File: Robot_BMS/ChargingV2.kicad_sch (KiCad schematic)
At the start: 11 parts, among them Q7 2N7002, U4 TPS54308DDCR

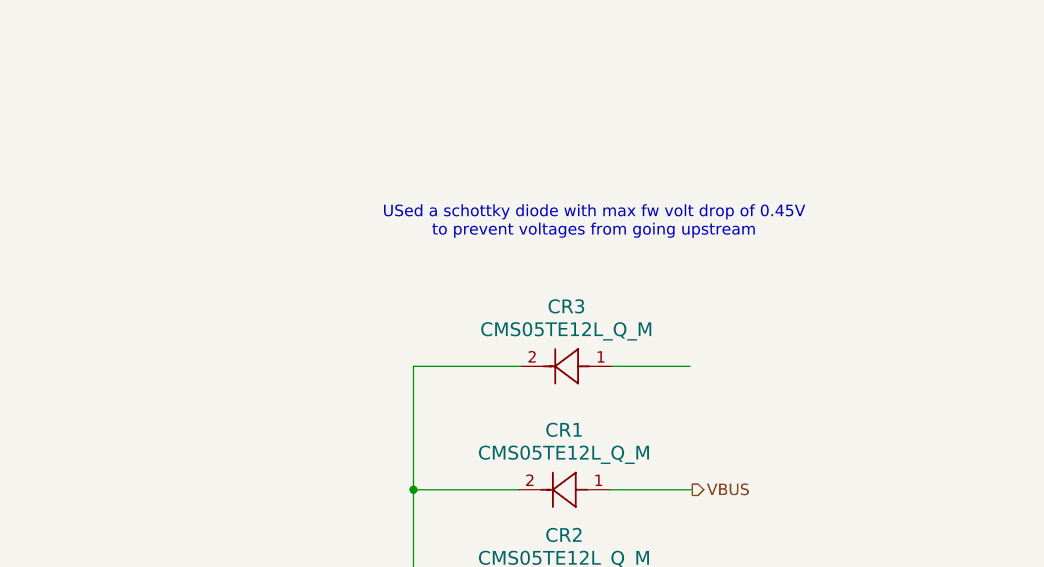
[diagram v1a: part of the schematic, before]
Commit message: battery management ic is being added
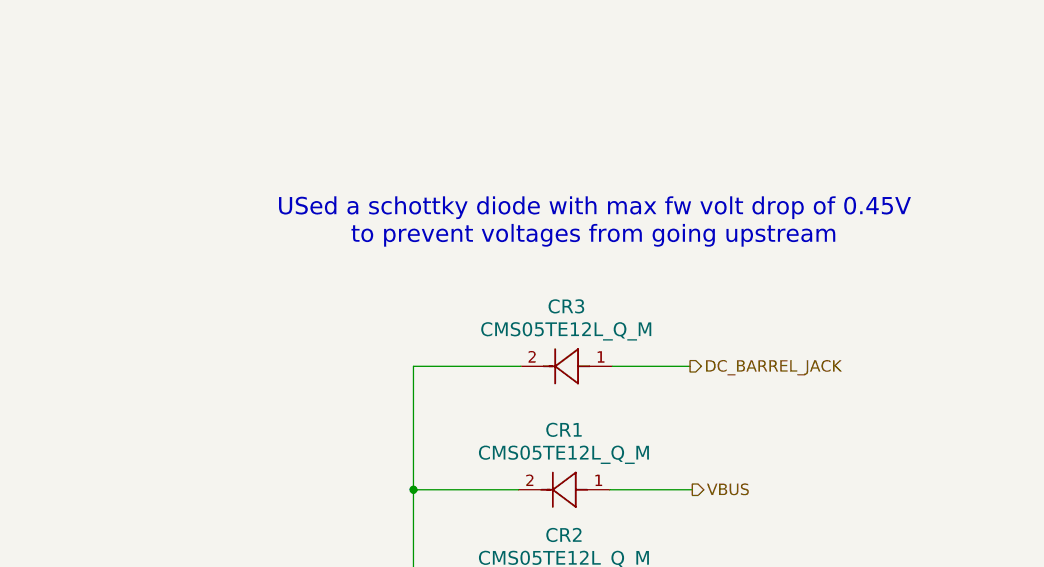
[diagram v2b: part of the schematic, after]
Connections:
- net DC_BARREL_JACK: now reaches CR3.1
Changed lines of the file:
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@@
 		(effects
 			(font
-				(size 1.27 1.27)
+				(size 1.905 1.905)
 			)
 		)
@@
 		)
 	)
+	(hierarchical_label "DC_BARREL_JACK"
+		(shape output)
+		(at 237.236 82.804 0)
+		(effects
+			(font
+				(size 1.27 1.27)
+			)
+			(justify left)
+		)
+	)

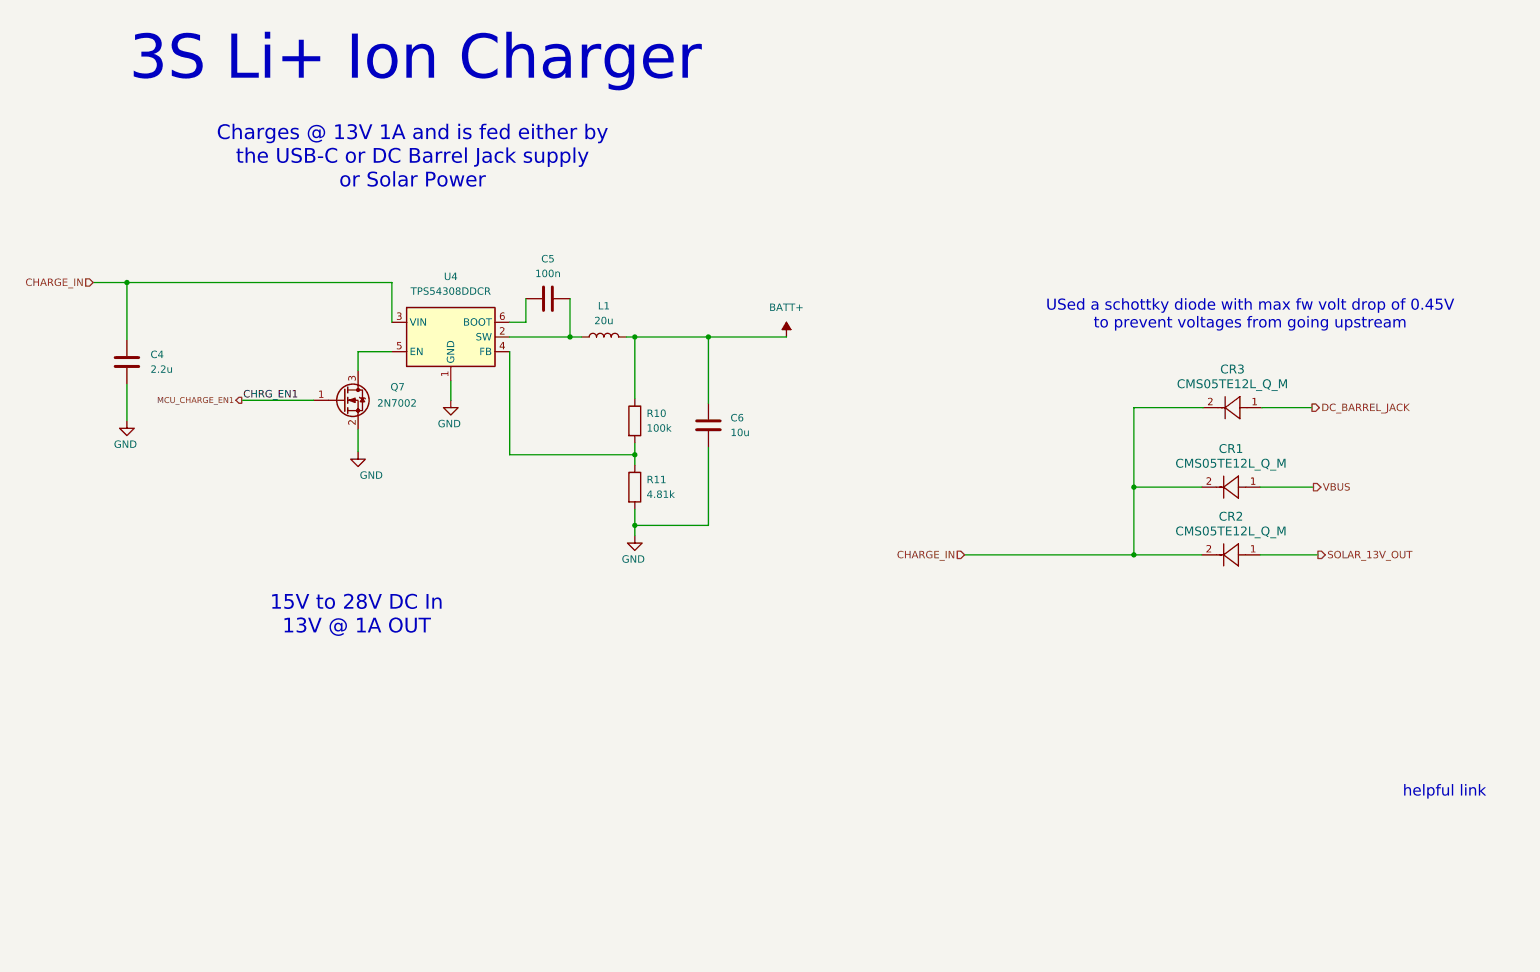
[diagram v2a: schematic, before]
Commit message: System drawing down on top schematic, will start inputting footprints
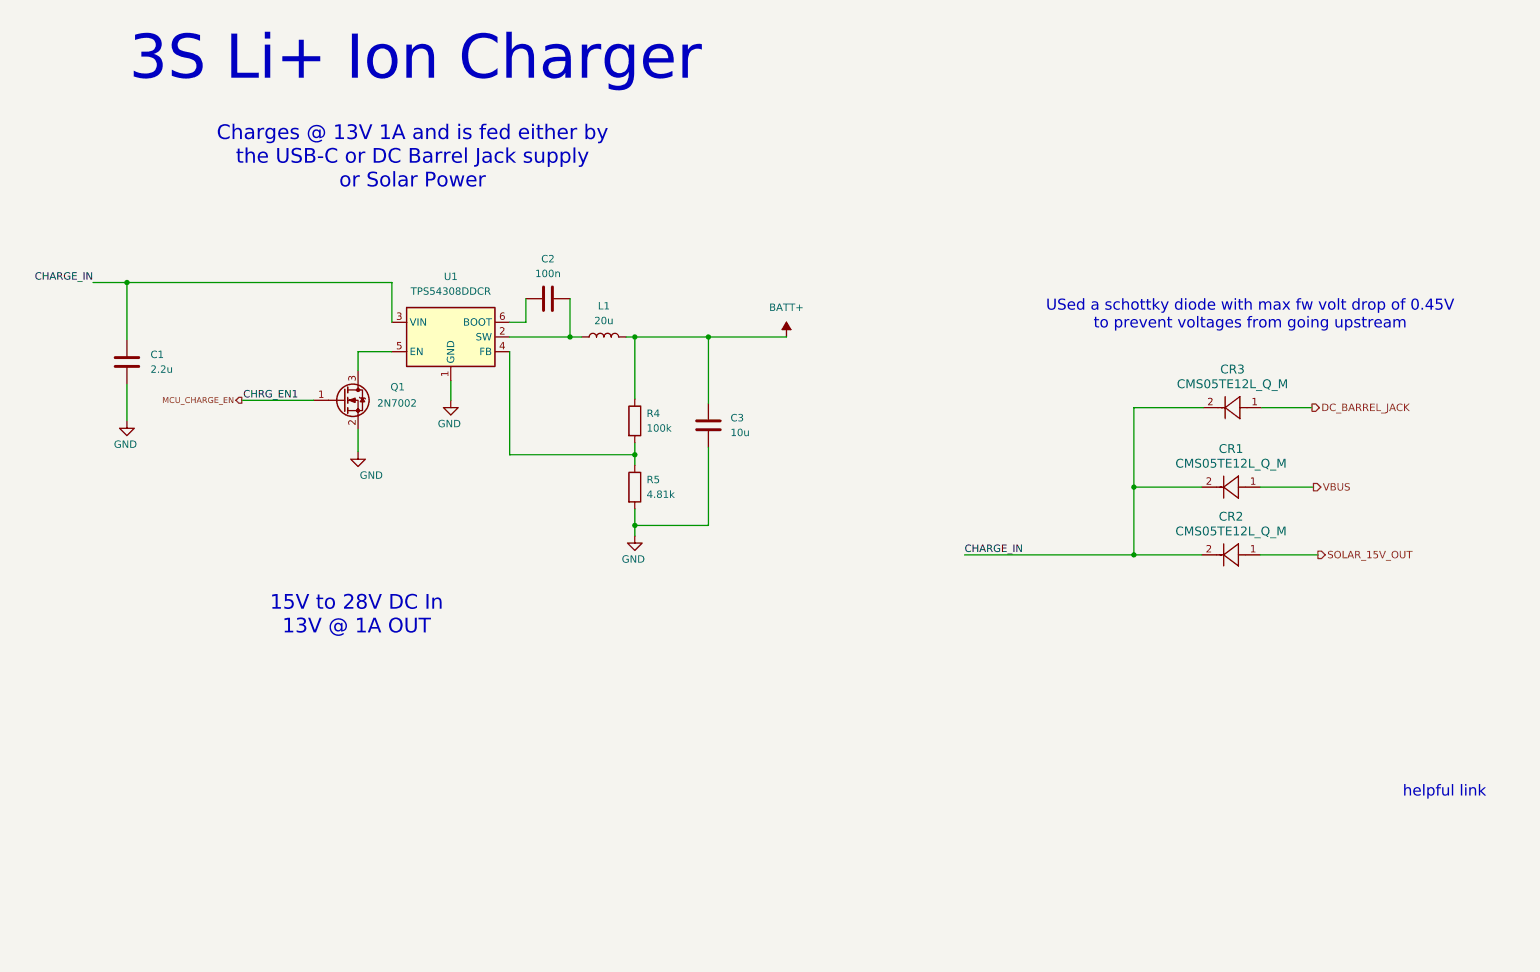
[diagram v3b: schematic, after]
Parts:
- renumbered C4 to C1, C5 to C2, C6 to C3, Q7 to Q1, R10 to R4, R11 to R5, U4 to U1
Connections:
- net MCU_CHARGE_EN1 renamed MCU_CHARGE_EN
- net SOLAR_13V_OUT renamed SOLAR_15V_OUT
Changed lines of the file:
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@@
 		)
 	)
-	(hierarchical_label "SOLAR_13V_OUT"
+	(label "CHARGE_IN"
+		(at 177.292 108.204 0)
+		(effects
+			(font
+				(size 1.27 1.27)
+			)
+			(justify left bottom)
+		)
+	)
+	(label "CHARGE_IN"
+		(at 26.924 61.214 180)
+		(effects
+			(font
+				(size 1.27 1.27)
+			)
+			(justify right bottom)
+		)
+	)
+	(hierarchical_label "SOLAR_15V_OUT"
 		(shape output)
 		(at 238.252 108.204 0)
@@
 		)
 	)
-	(hierarchical_label "MCU_CHARGE_EN1"
+	(hierarchical_label "MCU_CHARGE_EN"
 		(shape output)
 		(at 52.578 81.534 180)
@@
 			(font
 				(size 1.016 1.016)
-			)
-			(justify right)
-		)
-	)
-	(hierarchical_label "CHARGE_IN"
-		(shape input)
-		(at 177.292 108.204 180)
-		(effects
-			(font
-				(size 1.27 1.27)
 			)
 			(justify right)
@@
 		)
 	)
-	(hierarchical_label "CHARGE_IN"
-		(shape input)
-		(at 26.924 61.214 180)
-		(effects
-			(font
-				(size 1.27 1.27)
-			)
-			(justify right)
-		)
-	)
 	(symbol
 		(lib_id "Regulator_Switching:TPS54308")
@@
 		(dnp no)
 		(fields_autoplaced yes)
-		(property "Reference" "U4"
+		(property "Reference" "U1"
 			(at 88.646 60.198 0)
 			(effects
@@
 			(project ""
 				(path "/72551b1c-3d40-4199-8911-e5b015f4abec/31837631-dd5f-49d4-a8ae-a36c80dc2ea1"
-					(reference "U4")
+					(reference "U1")
 					(unit 1)
 				)
@@
 		(dnp no)
 		(fields_autoplaced yes)
-		(property "Reference" "C5"
+		(property "Reference" "C2"
 			(at 105.41 57.15 90)
 			(effects
@@
 			(project ""
 				(path "/72551b1c-3d40-4199-8911-e5b015f4abec/31837631-dd5f-49d4-a8ae-a36c80dc2ea1"
-					(reference "C5")
+					(reference "C2")
 					(unit 1)
 				)
@@
 		(dnp no)
 		(fields_autoplaced yes)
-		(property "Reference" "C6"
+		(property "Reference" "C3"
 			(at 136.906 84.5819 0)
 			(effects
@@
 			(project ""
 				(path "/72551b1c-3d40-4199-8911-e5b015f4abec/31837631-dd5f-49d4-a8ae-a36c80dc2ea1"
-					(reference "C6")
+					(reference "C3")
 					(unit 1)
 				)
@@
 		(dnp no)
 		(fields_autoplaced yes)
-		(property "Reference" "R11"
+		(property "Reference" "R5"
 			(at 122.428 95.2499 0)
 			(effects
@@
 			(project ""
 				(path "/72551b1c-3d40-4199-8911-e5b015f4abec/31837631-dd5f-49d4-a8ae-a36c80dc2ea1"
-					(reference "R11")
+					(reference "R5")
 					(unit 1)
 				)
@@
 		(dnp no)
 		(fields_autoplaced yes)
-		(property "Reference" "R10"
+		(property "Reference" "R4"
 			(at 122.428 83.8199 0)
 			(effects
@@
 			(project "Robot_BMS"
 				(path "/72551b1c-3d40-4199-8911-e5b015f4abec/31837631-dd5f-49d4-a8ae-a36c80dc2ea1"
-					(reference "R10")
+					(reference "R4")
 					(unit 1)
 				)
@@
 		(dnp no)
 		(fields_autoplaced yes)
-		(property "Reference" "C4"
+		(property "Reference" "C1"
 			(at 36.83 73.6599 0)
 			(effects
@@
 			(project "Robot_BMS"
 				(path "/72551b1c-3d40-4199-8911-e5b015f4abec/31837631-dd5f-49d4-a8ae-a36c80dc2ea1"
-					(reference "C4")
+					(reference "C1")
 					(unit 1)
 				)
@@
 		(on_board yes)
 		(dnp no)
-		(property "Reference" "Q7"
+		(property "Reference" "Q1"
 			(at 78.232 79.248 0)
 			(effects
@@
 			(project "Robot_BMS"
 				(path "/72551b1c-3d40-4199-8911-e5b015f4abec/31837631-dd5f-49d4-a8ae-a36c80dc2ea1"
-					(reference "Q7")
-					(unit 1)
-				)
+					(reference "Q1")
+					(unit 1)
+				)

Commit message: adding footprints and actual passive components
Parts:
- CR1, CR2, CR3: footprint M-FLAT_TOS -> RobotBMS:M-FLAT_TOS
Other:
- note added: "All standard Passive componenets are 0603 imperial"
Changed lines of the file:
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@@
+	)
+	(junction
+		(at 146.558 70.612)
+		(diameter 0)
+		(color 0 0 0 0)
 	)
 	(junction
@@
 		(color 0 0 0 0)
 	)
+	(junction
+		(at 72.39 61.214)
+		(diameter 0)
+		(color 0 0 0 0)
+	)
 	(wire
 		(pts
@@
 	(wire
 		(pts
+			(xy 51.816 81.534) (xy 65.024 81.534)
+		)
+		(stroke
+			(width 0)
+			(type default)
+		)
+	)
+	(wire
+		(pts
 			(xy 206.502 108.204) (xy 218.186 108.204)
 		)
@@
 	(wire
 		(pts
+			(xy 72.39 61.214) (xy 78.486 61.214)
+		)
+		(stroke
+			(width 0)
+			(type default)
+		)
+	)
+	(wire
+		(pts
 			(xy 98.806 73.152) (xy 98.806 90.932)
 		)
@@
 	(wire
 		(pts
-			(xy 52.578 81.534) (xy 65.024 81.534)
-		)
-		(stroke
-			(width 0)
-			(type default)
-		)
-	)
-	(wire
-		(pts
 			(xy 26.924 61.214) (xy 32.766 61.214)
 		)
@@
 	(wire
 		(pts
-			(xy 32.766 61.214) (xy 78.486 61.214)
+			(xy 32.766 61.214) (xy 72.39 61.214)
 		)
 		(stroke
@@
 		)
 	)
-	(label "CHRG_EN1"
-		(at 52.832 81.534 0)
+	(text "All standard Passive\ncomponenets are 0603 imperial"
+		(exclude_from_sim no)
+		(at 208.28 173.736 0)
 		(effects
 			(font
-				(size 1.27 1.27)
-			)
-			(justify left bottom)
+				(size 2.54 2.54)
+			)
 		)
 	)
@@
 	(hierarchical_label "MCU_CHARGE_EN"
 		(shape output)
-		(at 52.578 81.534 180)
+		(at 51.816 81.534 180)
 		(effects
 			(font
@@
 	)
 	(symbol
+		(lib_id "power:PWR_FLAG")
+		(at 72.39 61.214 180)
+		(unit 1)
+		(exclude_from_sim no)
+		(in_bom yes)
+		(on_board yes)
+		(dnp no)
+		(property "Reference" "#FLG03"
+			(at 72.39 63.119 0)
+			(effects
+				(font
+					(size 1.27 1.27)
+				)
+				(hide yes)
+			)
+		)
+		(property "Value" "PWR_FLAG"
+			(at 72.39 66.294 0)
+			(effects
+				(font
+					(size 1.27 1.27)
+				)
+			)
+		)
+		(property "Footprint" ""
+			(at 72.39 61.214 0)
+			(effects
+				(font
+					(size 1.27 1.27)
+				)
+				(hide yes)
+			)
+		)
+		(property "Datasheet" "~"
+			(at 72.39 61.214 0)
+			(effects
+				(font
+					(size 1.27 1.27)
+				)
+				(hide yes)
+			)
+		)
+		(property "Description" "Special symbol for telling ERC where power comes from"
+			(at 72.39 61.214 0)
+			(effects
+				(font
+					(size 1.27 1.27)
+				)
+				(hide yes)
+			)
+		)
+		(pin "1"
+		)
+		(instances
+			(project "Robot_BMS"
+				(path "/72551b1c-3d40-4199-8911-e5b015f4abec/31837631-dd5f-49d4-a8ae-a36c80dc2ea1"
+					(reference "#FLG03")
+					(unit 1)
+				)
+			)
+		)
+	)
+	(symbol
 		(lib_id "Device:C")
 		(at 105.41 64.008 90)
@@
 			)
 		)
-		(property "Footprint" "M-FLAT_TOS"
+		(property "Footprint" "RobotBMS:M-FLAT_TOS"
 			(at 218.186 108.204 0)
 			(effects
@@
 			)
 		)
-		(property "Footprint" "M-FLAT_TOS"
+		(property "Footprint" "RobotBMS:M-FLAT_TOS"
 			(at 218.186 96.52 0)
 			(effects
@@
 			)
 		)
-		(property "Footprint" "M-FLAT_TOS"
+		(property "Footprint" "RobotBMS:M-FLAT_TOS"
 			(at 218.44 82.804 0)
 			(effects
@@
 					(unit 1)
 				)
+			)
+		)
+	)
+	(symbol
+		(lib_id "power:PWR_FLAG")
+		(at 146.558 70.612 180)
+		(unit 1)
+		(exclude_from_sim no)
+		(in_bom yes)
+		(on_board yes)
+		(dnp no)
+		(property "Reference" "#FLG04"
+			(at 146.558 72.517 0)
+			(effects
+				(font
+					(size 1.27 1.27)
+				)
+				(hide yes)
+			)
+		)
+		(property "Value" "PWR_FLAG"
+			(at 146.558 75.692 0)
+			(effects
+				(font
+					(size 1.27 1.27)
+				)
+			)
+		)
+		(property "Footprint" ""
+			(at 146.558 70.612 0)
+			(effects
+				(font
+					(size 1.27 1.27)
+				)
+				(hide yes)
+			)
+		)
+		(property "Datasheet" "~"
+			(at 146.558 70.612 0)
+			(effects
+				(font
+					(size 1.27 1.27)
+				)
+				(hide yes)
+			)
+		)
+		(property "Description" "Special symbol for telling ERC where power comes from"
+			(at 146.558 70.612 0)
+			(effects
+				(font
+					(size 1.27 1.27)
+				)
+				(hide yes)
+			)
+		)
+		(pin "1"
+		)
+		(instances
+			(project "Robot_BMS"
+				(path "/72551b1c-3d40-4199-8911-e5b015f4abec/31837631-dd5f-49d4-a8ae-a36c80dc2ea1"
+					(reference "#FLG04")
+					(unit 1)
+				)

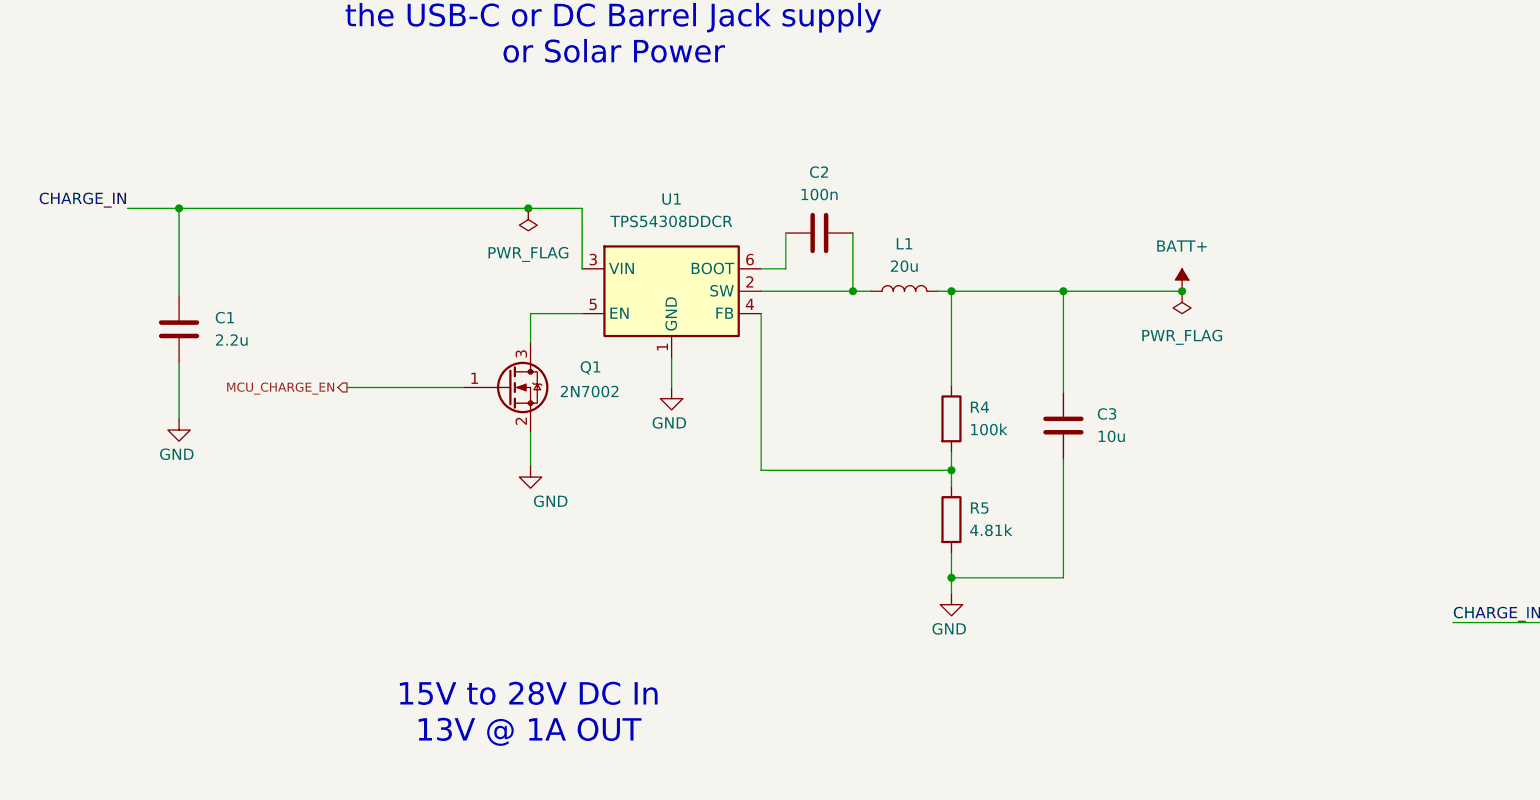
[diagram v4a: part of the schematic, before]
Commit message: adding footprints and actual passive components pt.2
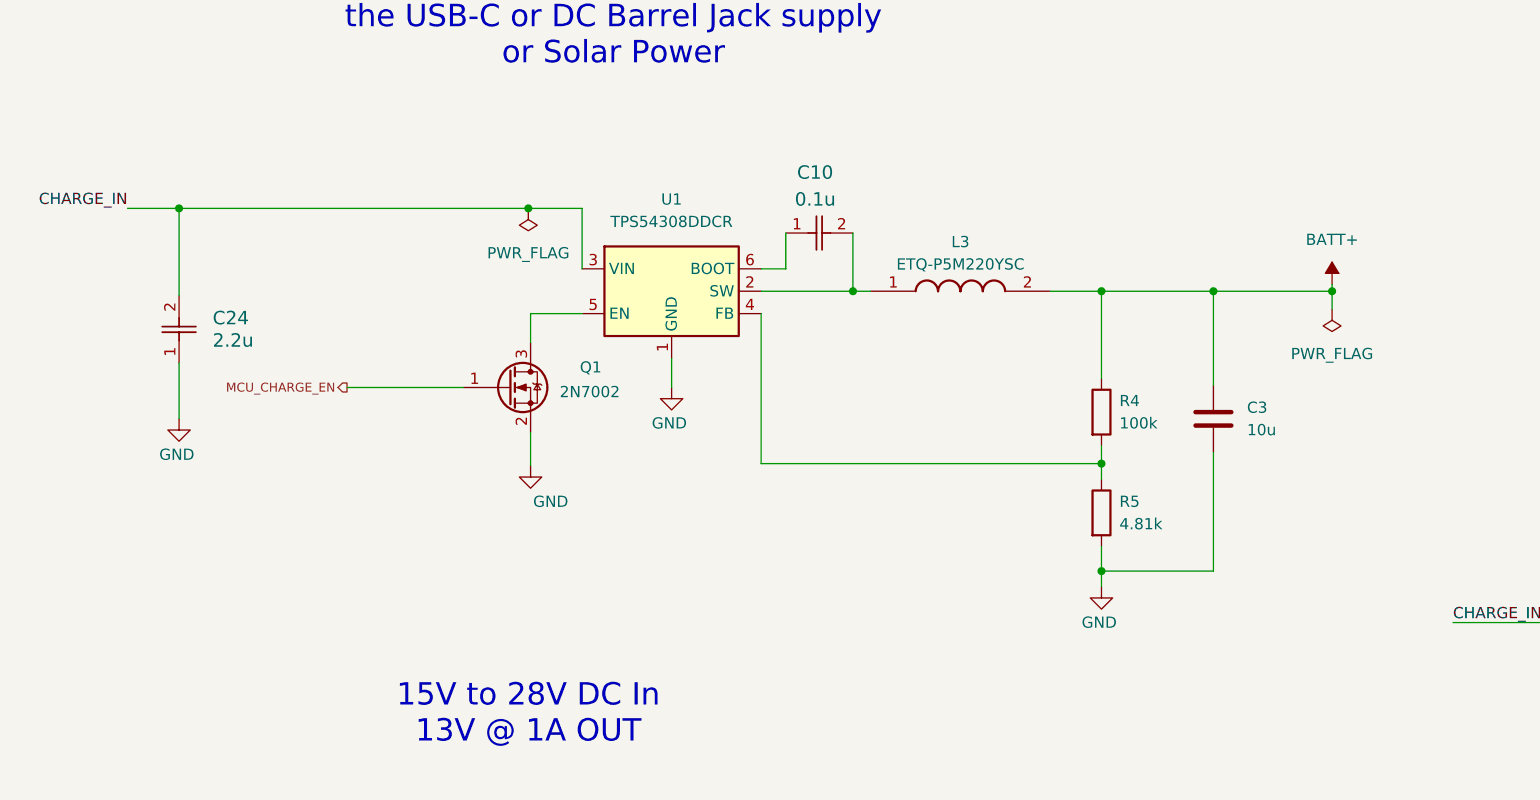
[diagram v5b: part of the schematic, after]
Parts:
- removed C1: 2.2u, symbol Device:C
- removed C2: 100n, symbol Device:C
- removed L1: 20u, symbol Device:L
- added C10: 0.1u, CAPC17595_87N_KEM, symbol C0603C104K5RACAUTO:C0603C104K5RACAUTO
- added C24: 2.2u, RobotBMS:CAP_GRM188R61H225KE11__MUR, symbol GRM188R61H225KE11D:GRM188R61H225KE11D
- added L3: ETQ-P5M220YSC, ETQP5M220YSC, symbol ETQ-P5M220YSC:ETQ-P5M220YSC
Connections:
- net BATT+: now also L3.2
- net CHARGE_IN: now also C24.2
- net GND: now also C24.1
- net at U1.2 (SW): now also C10.2, L3.1
- net at U1.6 (BOOT): now also C10.1
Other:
- moved on the sheet: C3, R4, R5
